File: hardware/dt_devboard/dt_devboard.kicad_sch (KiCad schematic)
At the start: 33 parts, among them IC1 MIMXRT1015CAF4A, IC2 ESP32-C3, Y1 Crystal_GND24

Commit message: added crystals for processor
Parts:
- added C? (x2): 4.7pF, symbol Device:C
- added C? (x2): 10pF, symbol Device:C
- added Y? (x2): Crystal_GND24, symbol Device:Crystal_GND24
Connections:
- net GND: now also C?.2, C?.2, C?.2, C?.2, Y?.2, Y?.4
- net at IC1.36 (RTC_XTALI): now also C?.1, Y?.2, Y?.3
- net at IC1.37 (RTC_XTALO): now also C?.1, Y?.1
- net at IC1.46 (XTALI): now also C?.1, Y?.3
- net at IC1.47 (XTALO): now also C?.1, Y?.1
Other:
- note added: "24 MHz Crystal"
- note added: "Add GPIO bank for unused GPIO to be reconfigured?"
- moved on the sheet: C1, C10, C11, C12, C13, C14, C2, C3, C4, C5, C6, C7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

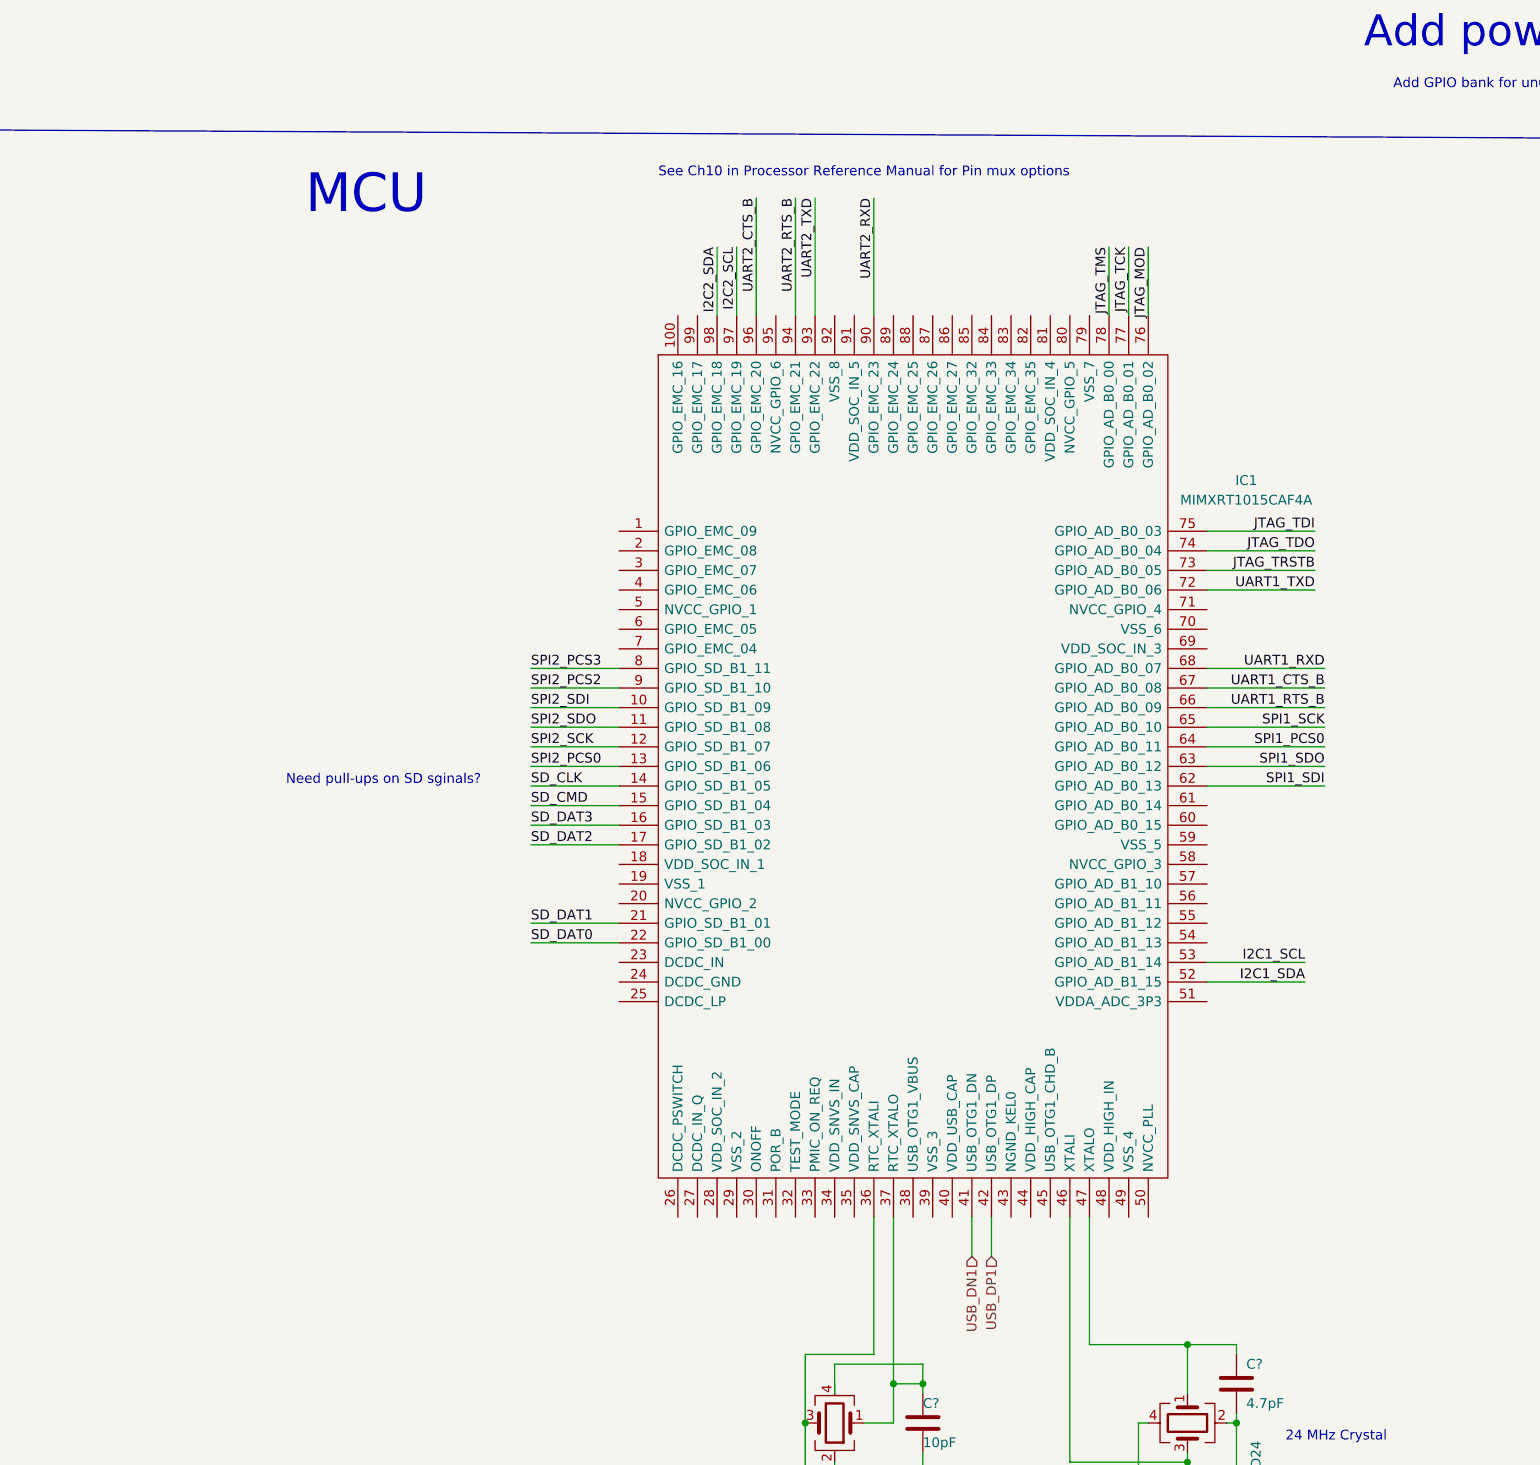
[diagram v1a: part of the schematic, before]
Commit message: added VSS GNDs
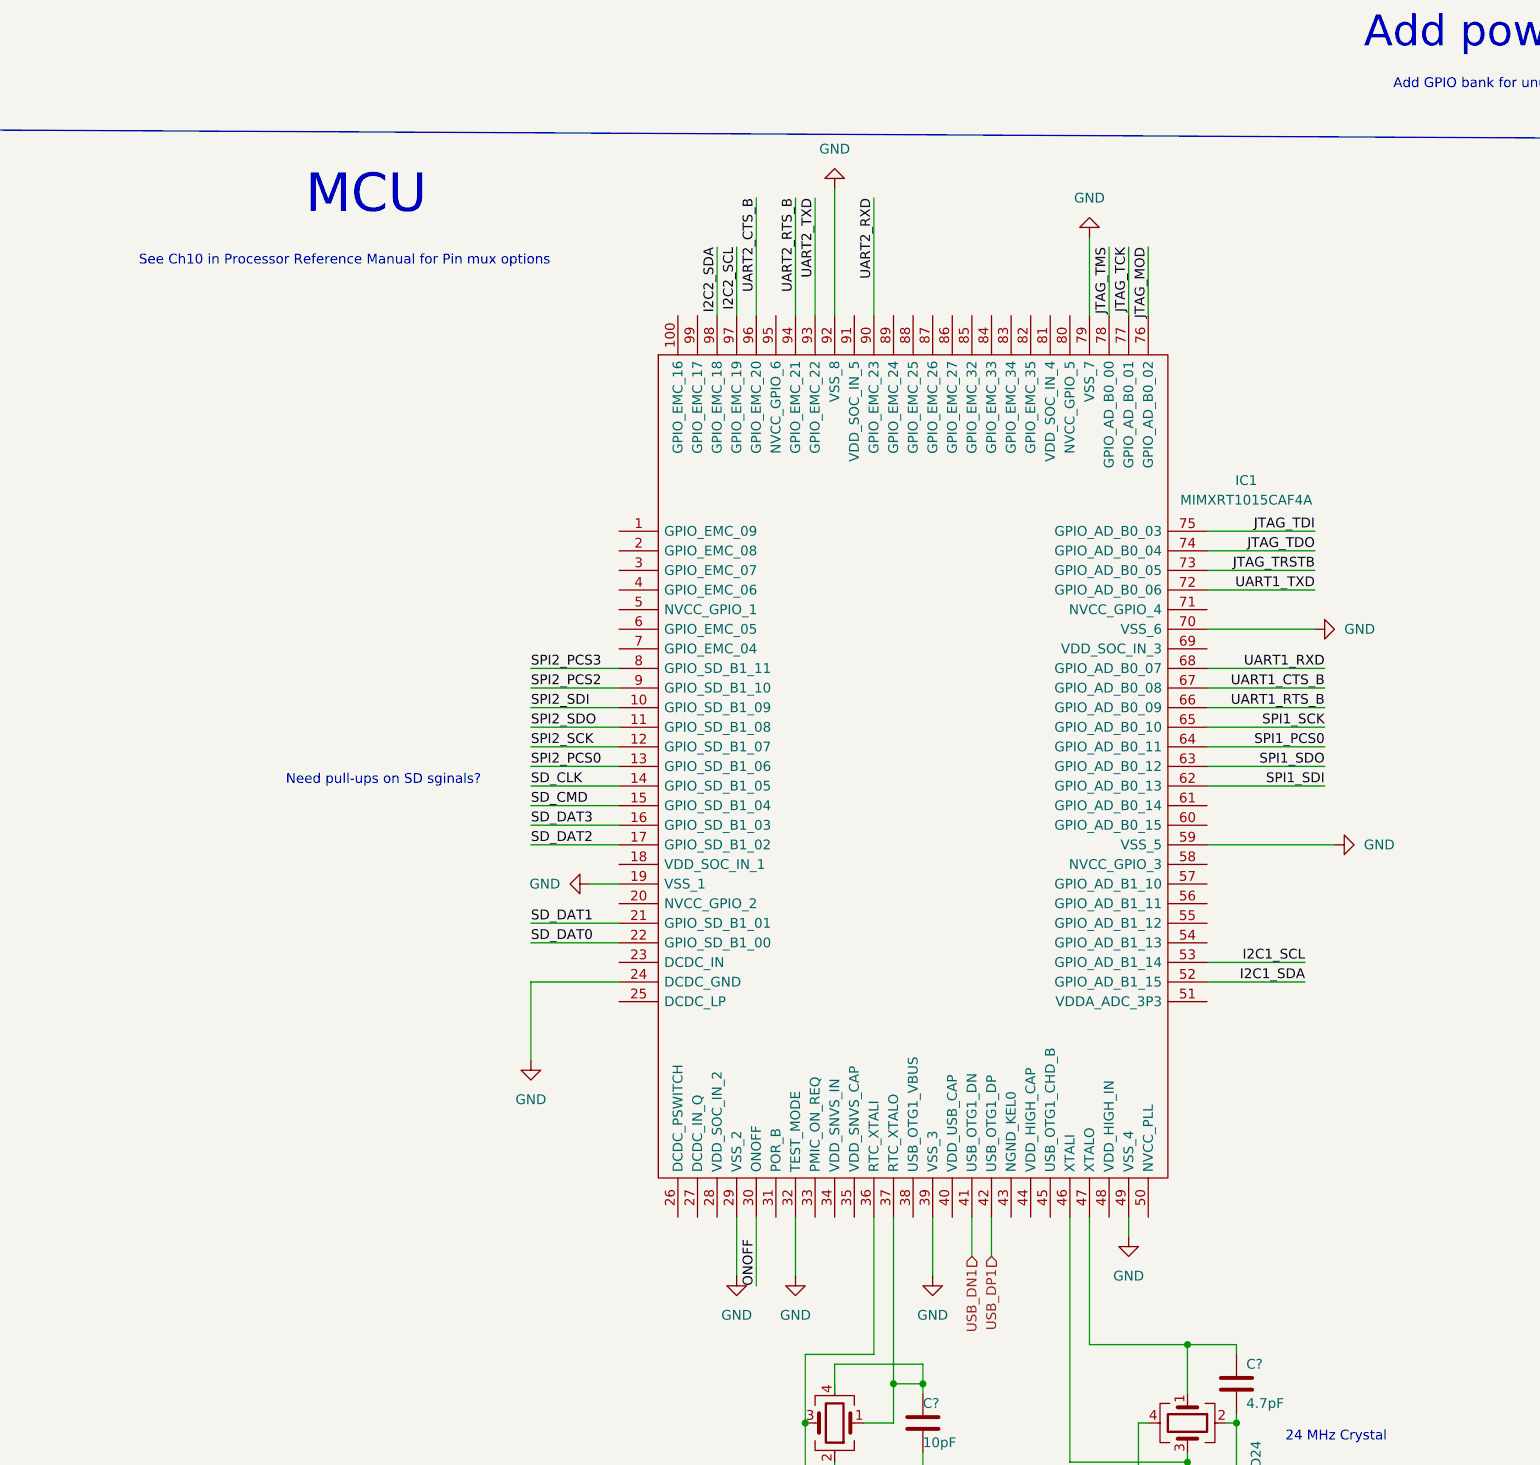
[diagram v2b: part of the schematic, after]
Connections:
- net GND: now also IC1.19 (VSS_1), IC1.24 (DCDC_GND), IC1.29 (VSS_2), IC1.32 (TEST_MODE), IC1.39 (VSS_3), IC1.49 (VSS_4), IC1.59 (VSS_5), IC1.70 (VSS_6), IC1.79 (VSS_7), IC1.92 (VSS_8)
- net ONOFF: now reaches IC1.30 (ONOFF)

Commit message: adding software packages
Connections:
- net GND: now also IC1.43 (NGND_KEL0)
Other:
- note added: "JTAG_TDI"
- note added: "JTAG_TDO"
- note added: "MCU interface signals:"
- note added: "Programming method?"
- note added: "RST"
- note added: "RX"
- note added: "SWD_CLK"
- note added: "SWD_DIO"
- note added: "TX"
- moved on the sheet: C?, J?, R?

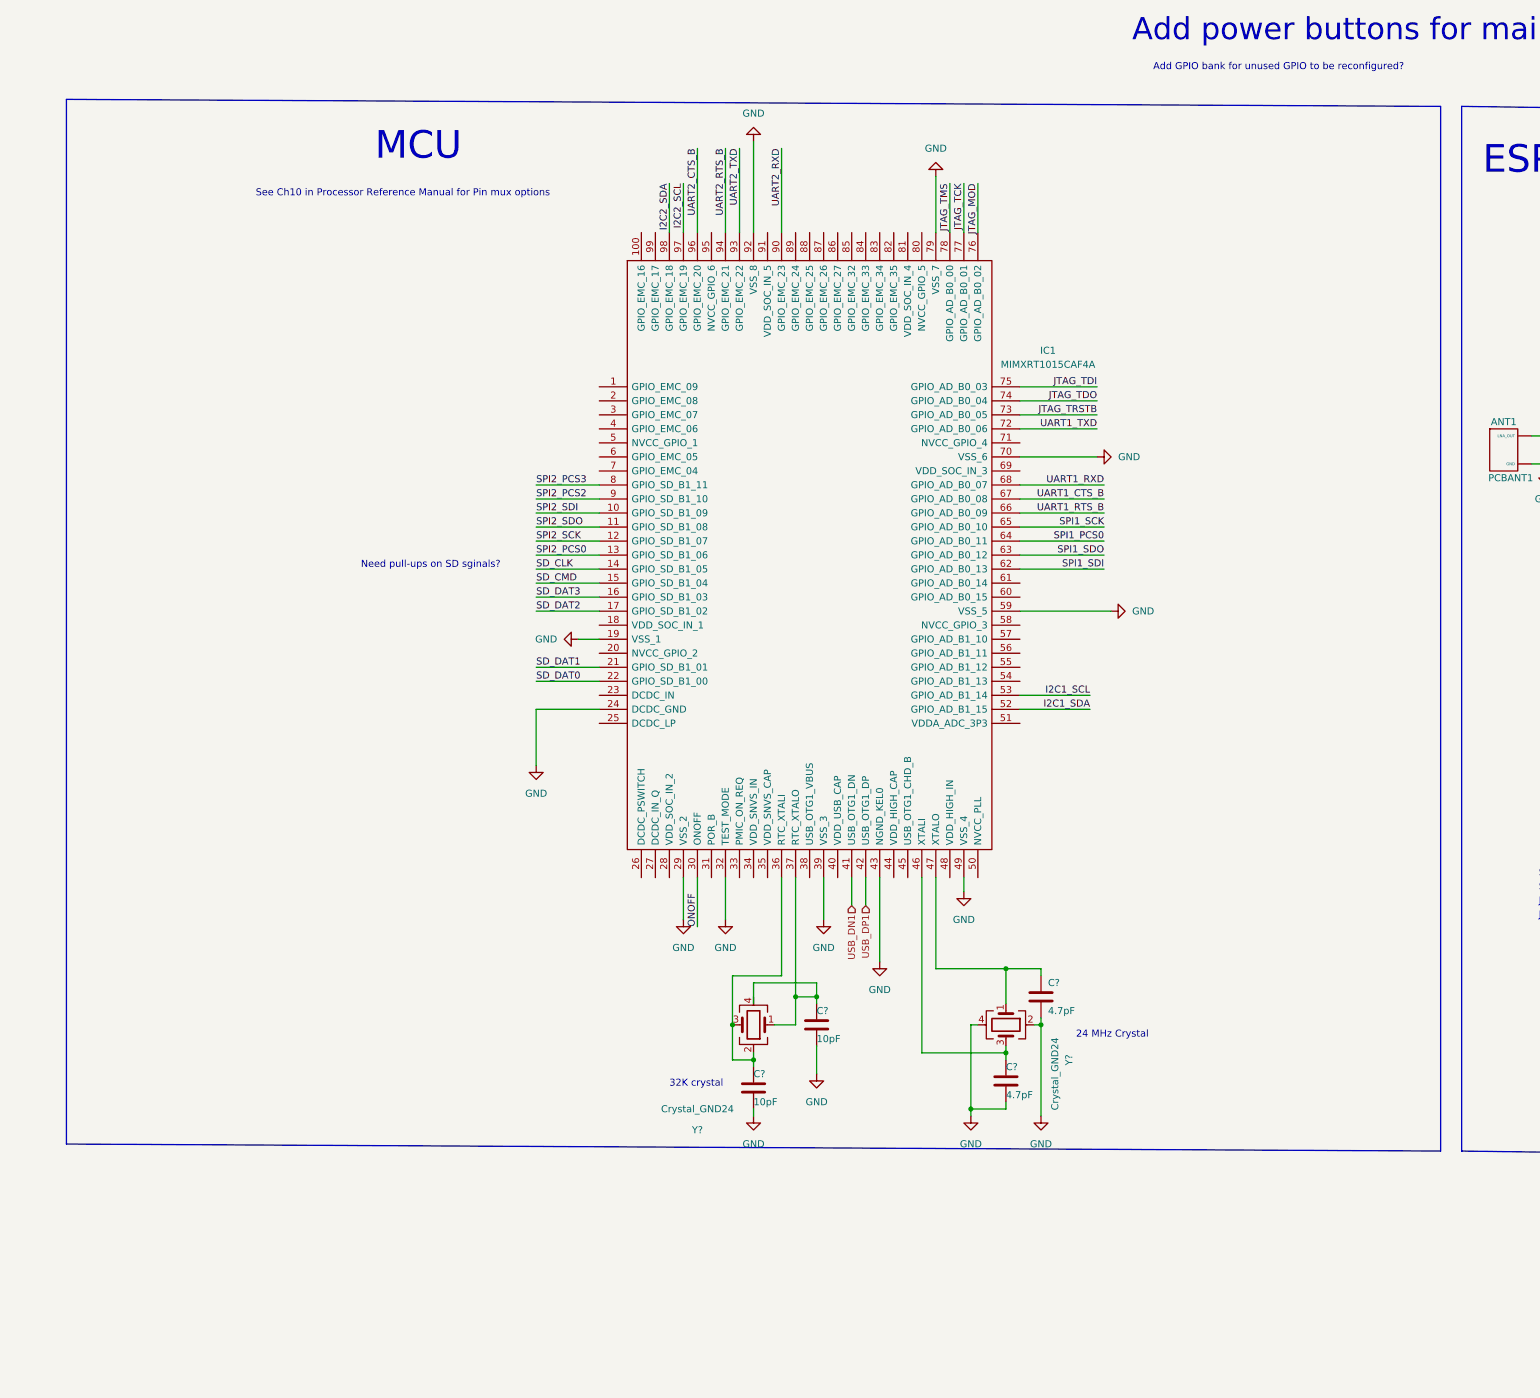
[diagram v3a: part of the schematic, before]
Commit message: adding digital and analog power domains on mcu
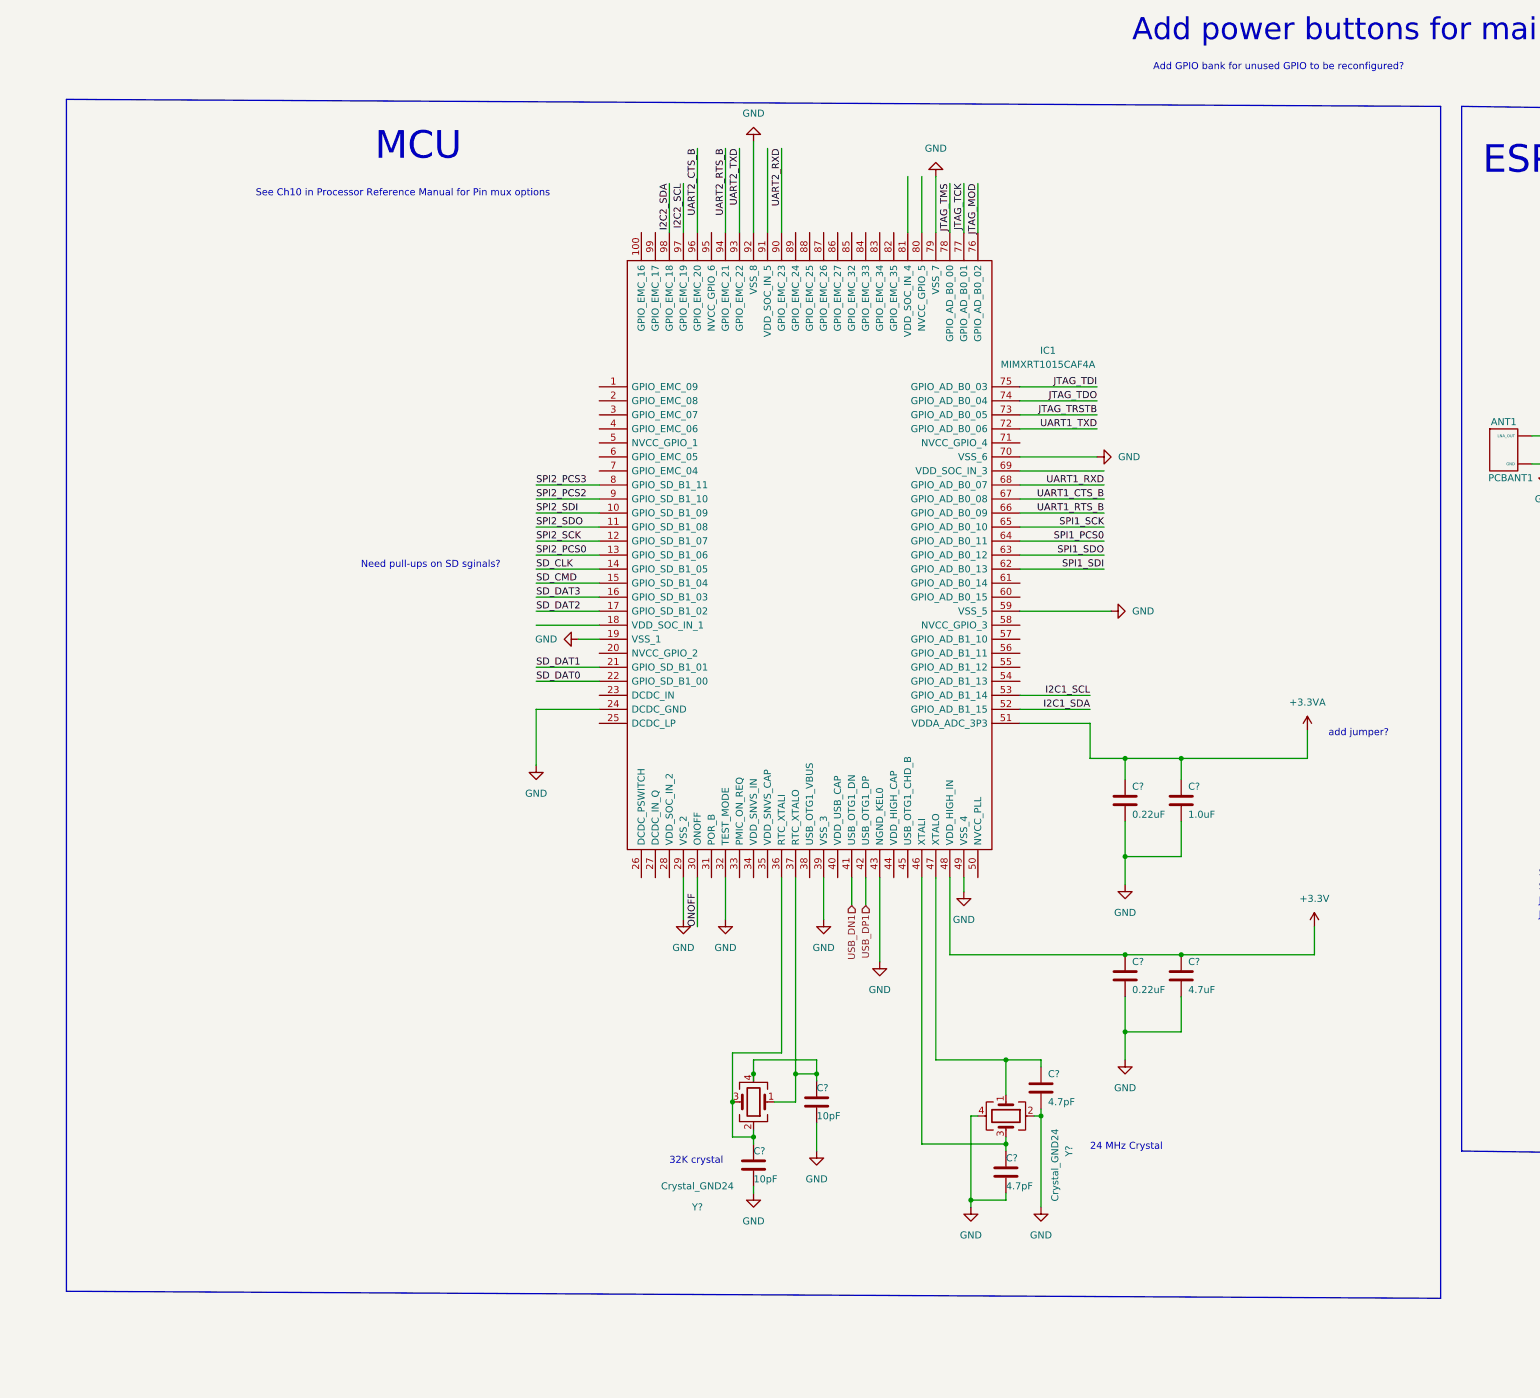
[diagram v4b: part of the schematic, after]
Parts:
- added C?: 4.7uF, symbol Device:C
- added C?: 1.0uF, symbol Device:C
- added C? (x2): 0.22uF, symbol Device:C
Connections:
- net +3V3: now also IC1.48 (VDD_HIGH_IN), C?.1, C?.1
- net GND: now also C?.2, C?.2, C?.2, C?.2
- net at C?.1, IC1.37 (RTC_XTALO), Y?.1: now also Y?.4
- net +3.3VA: now reaches IC1.51 (VDDA_ADC_3P3)
- net +3.3VA: now also C?.1, C?.1
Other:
- note added: "add jumper?"
- moved on the sheet: C?, Y?
